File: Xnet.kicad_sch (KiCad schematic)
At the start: 8 parts, among them J401 RJ12, J402 RJ12, U401 MAX485E

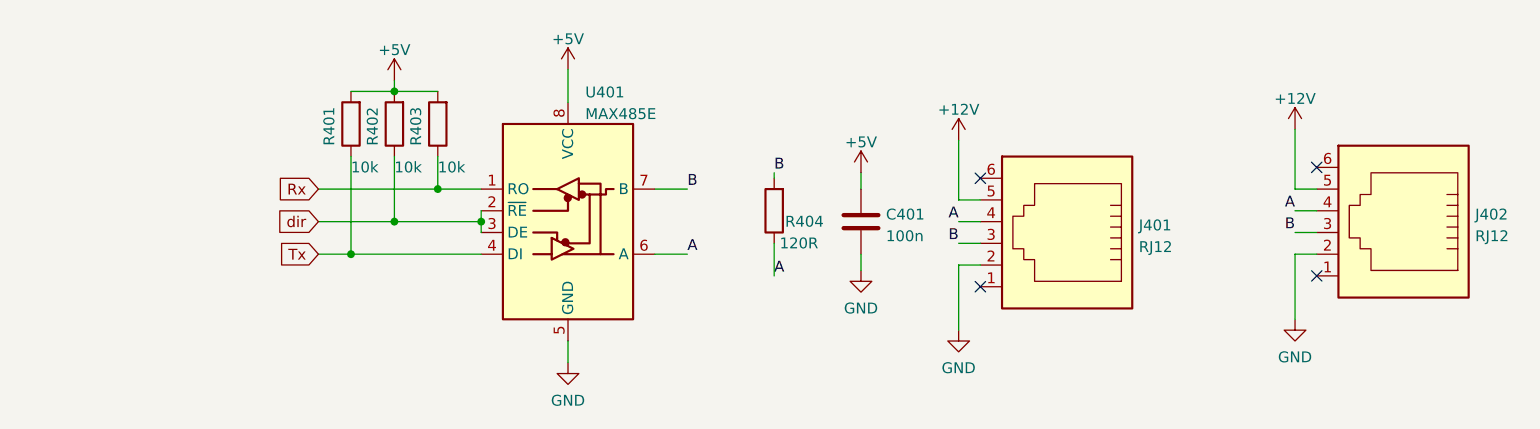
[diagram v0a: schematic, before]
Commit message: added ch340.sch
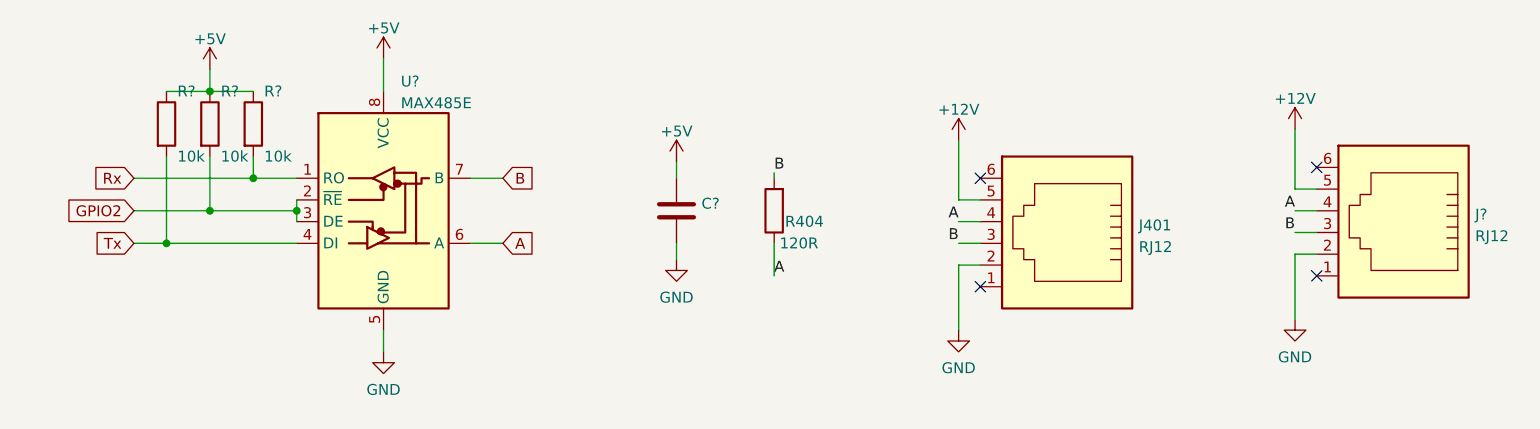
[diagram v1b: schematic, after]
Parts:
- removed C401: 100n, symbol Device:C
- removed J402: RJ12, symbol Connector:RJ12
- removed R401, R402, R403: 10k, symbol Device:R
- removed U401: MAX485E, symbol Interface_UART:MAX485E
- added C?: ~, symbol Device:C
- added J?: RJ12, Connector_RJ:RJ12_Amphenol_54601, symbol Connector:RJ12
- added R? (x3): 10k, Resistor_SMD:R_0402_1005Metric, symbol Device:R
- added U?: MAX485E, Package_SO:SOIC-8_3.9x4.9mm_P1.27mm, symbol Interface_UART:MAX485E
- J401: footprint (none) -> Connector_RJ:RJ12_Amphenol_54601
- R404: footprint (none) -> Resistor_SMD:R_0805_2012Metric
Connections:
- net +12V: now also J?.5
- net +5V: now also C?.1, R?.1, R?.1, R?.1, U?.8 (VCC)
- net A: now also J?.4, U?.6 (A)
- net B: now also J?.3, U?.7 (B)
- net GND: now also C?.2, J?.2, U?.5 (GND)
- net Rx: now also R?.2, U?.1 (RO)
- net Tx: now also R?.2, U?.4 (DI)
- new net GPIO2: R?.2, U?.2 (~{RE}), U?.3 (DE)

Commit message: minor update with partnumbers and footprints
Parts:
- C?: footprint (none) -> Capacitor_SMD:C_0603_1608Metric
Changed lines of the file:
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@@
       (effects (font (size 1.27 1.27)) hide)
     )
-    (property "Datasheet" "~" (id 3) (at 116.84 87.63 0)
+    (property "Datasheet" "C17437" (id 3) (at 116.84 87.63 0)
+      (effects (font (size 1.27 1.27)) hide)
+    )
+    (property "Field4" "" (id 4) (at 116.84 87.63 0)
       (effects (font (size 1.27 1.27)) hide)
     )
@@
       (effects (font (size 1.27 1.27)) (justify left))
     )
-    (property "Footprint" "" (id 2) (at 106.3752 91.44 0)
-      (effects (font (size 1.27 1.27)) hide)
-    )
+    (property "Footprint" "Capacitor_SMD:C_0603_1608Metric" (id 2) (at 106.3752 91.44 0)
+      (effects (font (size 1.27 1.27)) hide)
+    )

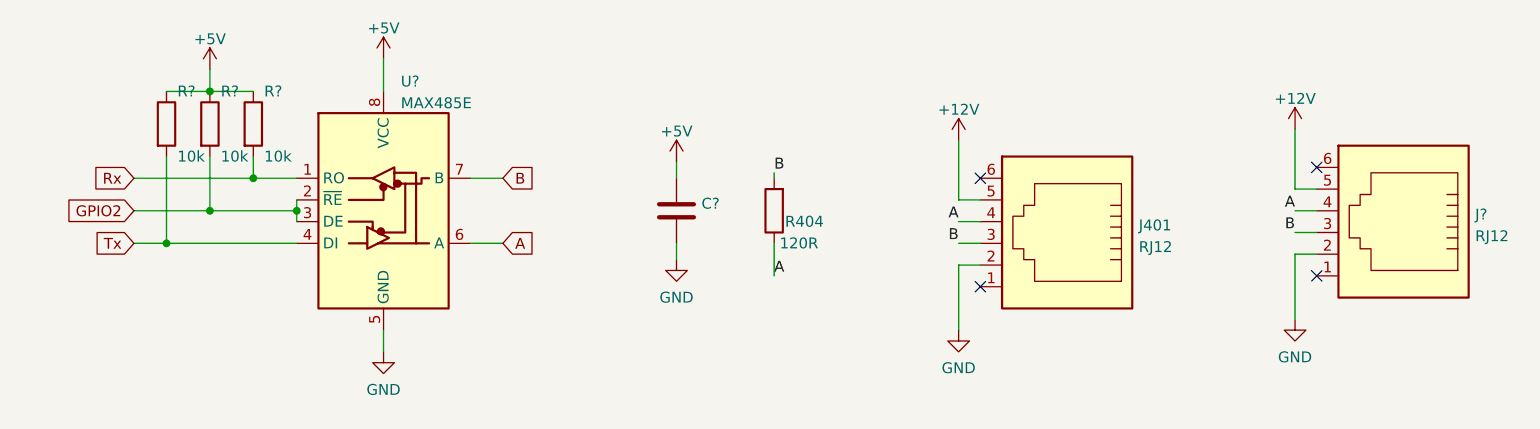
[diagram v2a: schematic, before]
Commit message: added hierarchial labels to some schematics
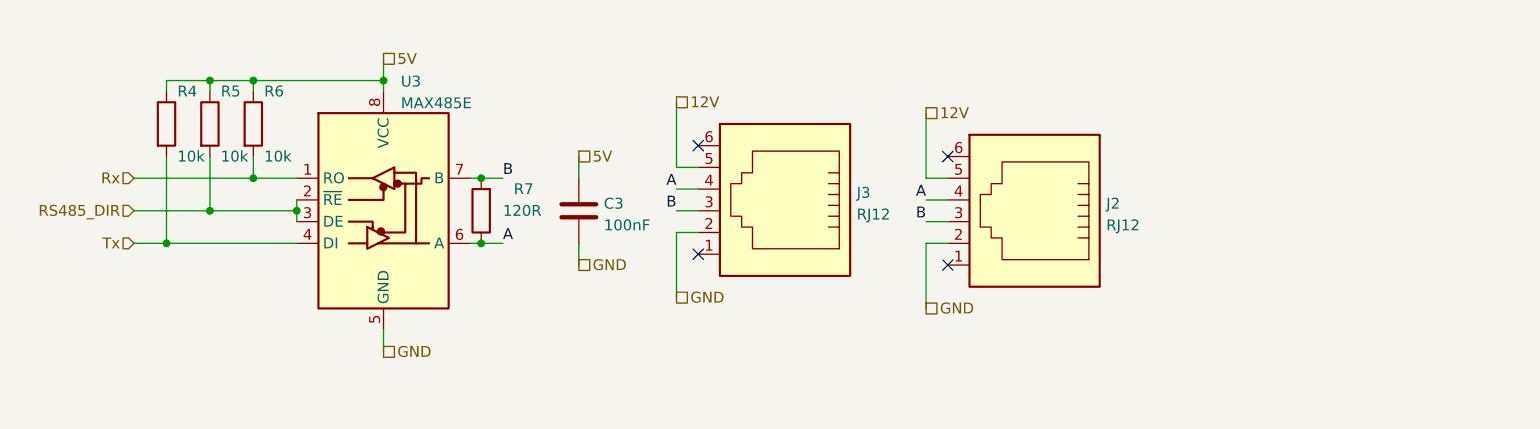
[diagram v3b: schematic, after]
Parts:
- removed J?: RJ12, Connector_RJ:RJ12_Amphenol_54601, symbol Connector:RJ12
- added J2: RJ12, Connector_RJ:RJ12_Amphenol_54601, symbol Connector:RJ12
- C3: renamed from C?; value ~ -> 100nF
- gave numbers to parts that had none: 4
- renumbered J401 to J3, R404 to R7
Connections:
- net A: now also J2.4
- net B: now also J2.3
- net GND: now also J2.2
- net +12V renamed 12V
- net 12V: now also J2.5
- net +5V renamed 5V
- net GPIO2 renamed RS485_DIR
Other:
- moved on the sheet: C3, J3, R7
